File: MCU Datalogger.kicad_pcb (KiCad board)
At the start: 2 copper layers, 0 parts

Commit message: setup of pcbnew
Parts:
- added BT1: Battery_Cell, Connector_PinHeader_2.54mm:PinHeader_1x02_P2.54mm_Vertical, F.Cu at (160.0, 89.1)
- added C1: 22pF, Capacitor_SMD:C_0805_2012Metric, F.Cu at (155.5, 88.3)
- added C2: 22pF, Capacitor_SMD:C_0805_2012Metric, F.Cu at (155.5, 91.4)
- added C3: 0.1uF, Capacitor_SMD:C_0805_2012Metric, F.Cu at (155.5, 94.4)
- added C4: 0.1u, Capacitor_SMD:C_0805_2012Metric, F.Cu at (155.5, 97.4)
- added C5: 100 nF, Capacitor_SMD:CP_Elec_3x5.3, F.Cu at (161.1, 96.4)
- added D1: LED, LED_SMD:LED_0805_2012Metric, F.Cu at (164.6, 88.4)
- added D2: LED, LED_SMD:LED_0805_2012Metric, F.Cu at (164.6, 91.4)
- added H1: MountingHole, MountingHole:MountingHole_2.1mm, F.Cu at (137.6, 89.7)
- added H2: MountingHole, MountingHole:MountingHole_2.1mm, F.Cu at (137.6, 95.5)
- added H3: MountingHole, MountingHole:MountingHole_2.1mm, F.Cu at (137.6, 101.2)
- added H4: MountingHole, MountingHole:MountingHole_2.1mm, F.Cu at (137.6, 107.0)
- added J1: Conn_01x04_Pin, Connector_PinHeader_2.54mm:PinHeader_1x04_P2.54mm_Vertical, F.Cu at (175.8, 89.1)
- added J2: Conn_01x04_Pin, Connector_PinHeader_2.54mm:PinHeader_1x04_P2.54mm_Vertical, F.Cu at (180.4, 89.1)
- added J3: Conn_01x09_Pin, Connector_PinHeader_2.54mm:PinHeader_1x09_P2.54mm_Vertical, F.Cu at (171.2, 89.1)
- added J4: Conn_02x03_Odd_Even, Connector_PinHeader_2.54mm:PinHeader_2x03_P2.54mm_Vertical, F.Cu at (175.8, 101.3)
- added R1: 10k, Resistor_SMD:R_0805_2012Metric, F.Cu at (142.6, 88.3)
- added R2: 330, Resistor_SMD:R_0805_2012Metric, F.Cu at (142.6, 91.3)
- added R3: 4.7k, Resistor_SMD:R_0805_2012Metric, F.Cu at (142.6, 94.2)
- added R4: 4.7k, Resistor_SMD:R_0805_2012Metric, F.Cu at (142.6, 97.2)
- added R5: 10k, Resistor_SMD:R_0805_2012Metric, F.Cu at (142.6, 100.1)
- added R6: 10k, Resistor_SMD:R_0805_2012Metric, F.Cu at (142.6, 103.1)
- added R7: 330, Resistor_SMD:R_0805_2012Metric, F.Cu at (142.6, 106.0)
- added U1: 24LC1025, Package_SO:SOIC-8_3.9x4.9mm_P1.27mm, F.Cu at (149.1, 90.2)
- added U2: DS1337S_, ds1337s:SOIC127P600X175-8N, F.Cu at (161.8, 113.0)
- added U3: 24LC1025, Package_SO:SOIC-8_3.9x4.9mm_P1.27mm, F.Cu at (149.1, 96.8)
- added U4: ATMEGA328P-AU, footprints:TQFP32_32A_MCH, F.Cu at (150.7, 106.0)
- added Y1: 32.768 KHZ, Crystal:Crystal_SMD_5032-2Pin_5.0x3.2mm_HandSoldering, F.Cu at (161.8, 102.4)
- added Y2: 16 MHZ, Crystal:Crystal_SMD_5032-2Pin_5.0x3.2mm_HandSoldering, F.Cu at (161.8, 107.3)

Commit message: placed components
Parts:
- moved H4 46.5 mm to (179.8, 87.6)
- moved H3 44.4 mm to (179.8, 114.8)
- moved J3 38.2 mm to (142.2, 114.0), turned to 90 degrees
- moved R7 30.2 mm to (171.3, 96.5)
- moved R2 30.1 mm to (171.3, 100.3)
- moved R4 29.7 mm to (171.3, 89.4)
- moved J2 28.0 mm to (167.6, 114.0), turned to 90 degrees
- moved R3 24.8 mm to (167.0, 89.4), turned to 180 degrees
- moved Y1 23.8 mm to (138.2, 105.7), turned to 90 degrees
- moved BT1 22.5 mm to (138.3, 95.0)
- moved H2 19.3 mm to (137.7, 114.8)
- moved U2 16.9 mm to (145.7, 107.7)
- moved R5 16.6 mm to (156.6, 109.2)
- moved C2 16.2 mm to (162.6, 105.9), turned to 180 degrees
- moved C1 15.9 mm to (162.6, 102.6), turned to 180 degrees
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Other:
- board outline added: 47.5 x 32.5 mm

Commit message: Routing done and fixed the drc errors successfully
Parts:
- added REF**: KiCad-Logo2_5mm_SilkScreen, Symbol:KiCad-Logo2_5mm_SilkScreen, F.Cu at (170.5, 108.8)
- turned D1 to 180 degrees
- turned D2 to 180 degrees
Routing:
- net GND: track 0.00 -> 147.4 mm, vias 0 -> 6
- net /SCK: track 0.00 -> 145.7 mm, vias 0 -> 7
- net /vcc: track 0.00 -> 133.1 mm
- net /SDA: track 0.00 -> 81.0 mm, vias 0 -> 5
- net Net-(BT1-+): track 0.00 -> 69.6 mm, vias 0 -> 1
- net /RESET: track 0.00 -> 51.4 mm, vias 0 -> 3
- net /MISO: track 0.00 -> 46.7 mm, vias 0 -> 1
- net /MOSI: track 0.00 -> 46.3 mm, vias 0 -> 1
- net /D2: track 0.00 -> 42.8 mm, vias 0 -> 1
- net /TX: track 0.00 -> 34.6 mm, vias 0 -> 1
- net /RX: track 0.00 -> 33.4 mm, vias 0 -> 1
- net /D3: track 0.00 -> 31.1 mm, vias 0 -> 1
- net /D4: track 0.00 -> 29.9 mm, vias 0 -> 1
- net Net-(U4-PB6(PCINT6/XTAL1/TOSC1)): track 0.00 -> 22.8 mm
- net /D5: track 0.00 -> 16.5 mm, vias 0 -> 1
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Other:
- outline, holes or cut-outs redrawn

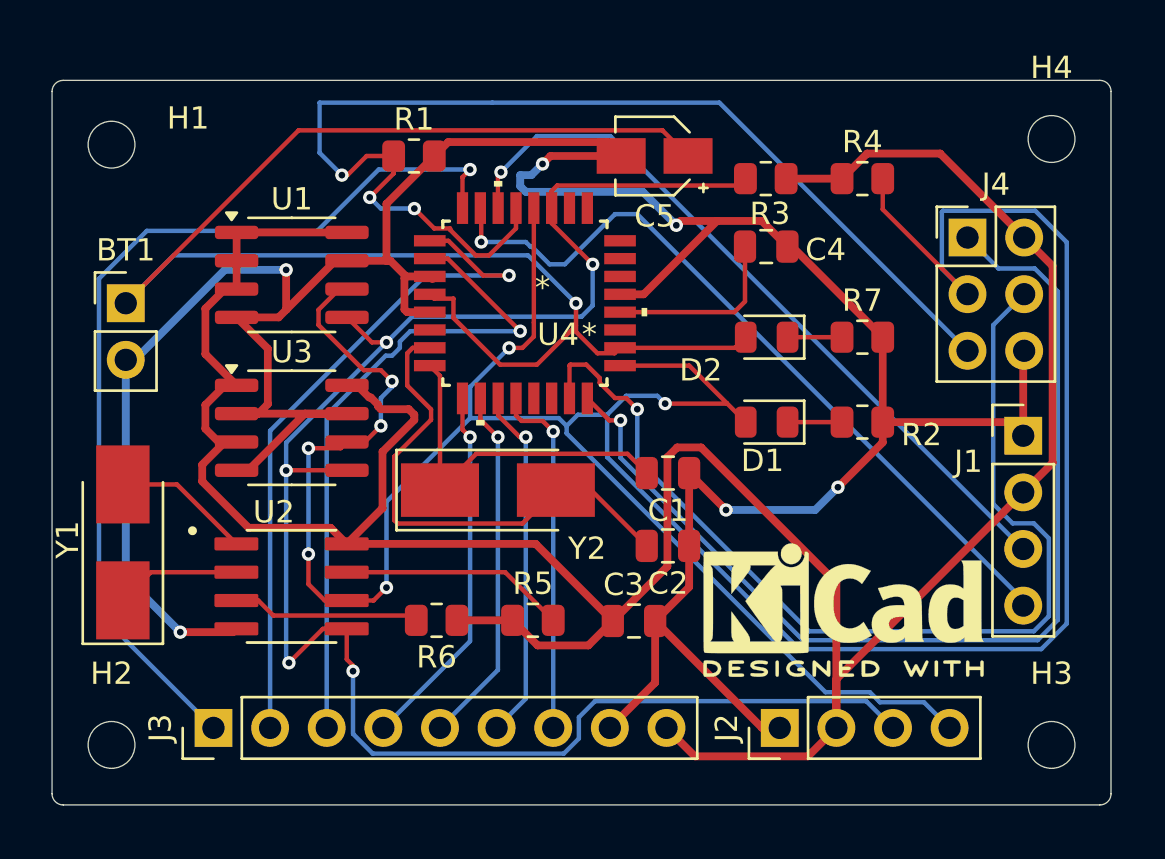
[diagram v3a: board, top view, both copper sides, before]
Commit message: copper fill and drc and refining the edge cuts completed
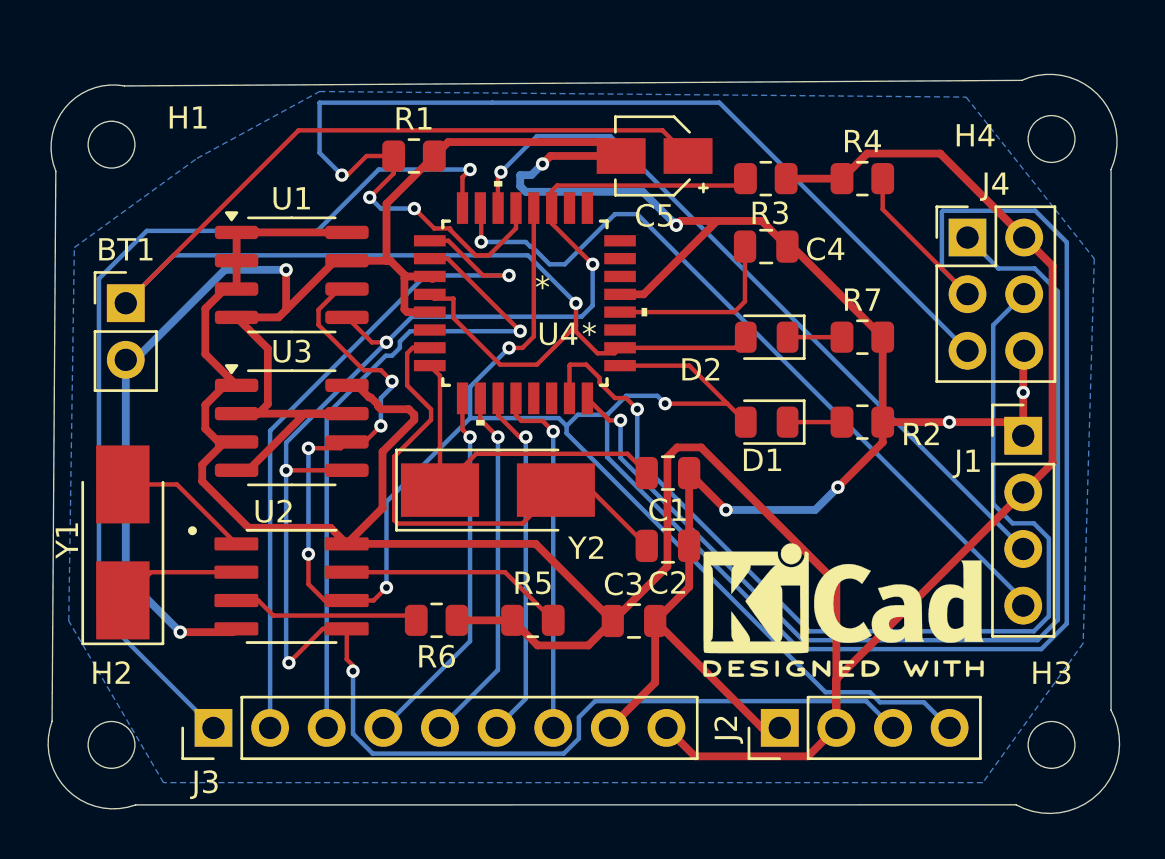
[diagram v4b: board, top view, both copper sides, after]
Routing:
- net GND: vias 6 -> 8
- added copper zone on B.Cu, net GND
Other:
- board size 47.5 x 32.5 mm -> 48.1 x 33.1 mm
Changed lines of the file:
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@@
 		(tags "Through hole pin header THT 1x09 2.54mm single row")
 		(property "Reference" "J3"
-			(at 0 -2.38 90)
+			(at -2.454 -0.34 180)
 			(layer "F.SilkS")
 			(effects
@@
 		(tags "mounting hole 2.1mm no annular")
 		(property "Reference" "H4"
-			(at 0 -3.2 0)
+			(at -3.432 -0.13 0)
 			(layer "F.SilkS")
 			(effects
@@
 	)
 	(gr_arc
-		(start 135 85.5)
-		(mid 135.146447 85.146447)
-		(end 135.5 85)
+		(start 182.5 113.25)
+		(mid 181.961345 116.96866)
+		(end 178.240926 117.495031)
 		(stroke
 			(width 0.05)
@@
 		(layer "Edge.Cuts")
 	)
-	(gr_line
-		(start 182 85)
-		(end 135.5 85)
+	(gr_arc
+		(start 138.75 117.5)
+		(mid 135.679513 116.817748)
+		(end 135.001326 113.74636)
 		(stroke
 			(width 0.05)
@@
 	)
 	(gr_line
-		(start 182.5 117)
-		(end 182.5 85.5)
+		(start 178.5 85)
+		(end 138.25 85.25)
 		(stroke
 			(width 0.05)
@@
 		(layer "Edge.Cuts")
 	)
-	(gr_arc
-		(start 182 85)
-		(mid 182.353553 85.146447)
-		(end 182.5 85.5)
+	(gr_line
+		(start 182.5 113.25)
+		(end 182.5 89)
 		(stroke
 			(width 0.05)
@@
 	)
 	(gr_arc
-		(start 135.5 117.5)
-		(mid 135.146447 117.353553)
-		(end 135 117)
+		(start 135.168862 89.072487)
+		(mid 135.573848 86.2459)
+		(end 138.25 85.25)
 		(stroke
 			(width 0.05)
@@
 	)
 	(gr_line
-		(start 135 85.5)
-		(end 135 117)
+		(start 135.168863 89.072487)
+		(end 135.001326 113.746364)
 		(stroke
 			(width 0.05)
@@
 	)
 	(gr_line
-		(start 135.5 117.5)
-		(end 182 117.5)
+		(start 138.75 117.5)
+		(end 178.240926 117.495031)
 		(stroke
 			(width 0.05)
@@
 	)
 	(gr_arc
-		(start 182.5 117)
-		(mid 182.353553 117.353553)
-		(end 182 117.5)
+		(start 178.5 85)
+		(mid 181.886001 85.613999)
+		(end 182.5 89)
 		(stroke
 			(width 0.05)
@@
 	)
 	(segment
+		(start 178.562 99)
+		(end 178.562 97.17181)
+		(width 0.35)
+		(layer "F.Cu")
+		(net 2)
+	)
+	(segment
 		(start 168.195 92.456)
 		(end 172.259 96.52)
@@
 	)
 	(segment
+		(start 175.25 100.33)
+		(end 177.952 100.33)
+		(width 0.35)
+		(layer "F.Cu")
+		(net 2)
+	)
+	(segment
 		(start 161.5384 94.596001)
 		(end 164.829401 91.305)
@@
 	(segment
 		(start 178.562 100.94)
-		(end 178.562 97.17181)
+		(end 178.562 99)
 		(width 0.35)
 		(layer "F.Cu")
@@
 	(segment
 		(start 172.259 100.33)
-		(end 177.952 100.33)
+		(end 175.25 100.33)
 		(width 0.35)
 		(layer "F.Cu")
@@
 	)
 	(via
+		(at 175.25 100.33)
+		(size 0.6)
+		(drill 0.3)
+		(layers "F.Cu" "B.Cu")
+		(net 2)
+	)
+	(via
 		(at 165.23 104.27)
 		(size 0.6)
@@
 		(net 2)
 	)
+	(via
+		(at 178.562 99)
+		(size 0.6)
+		(drill 0.3)
+		(layers "F.Cu" "B.Cu")
+		(net 2)
+	)
 	(segment
 		(start 156.5 89.25)
@@
 		(net 26)
 	)
+	(zone
+		(net 2)
+		(net_name "GND")
+		(layer "B.Cu")
+		(hatch full 0.5)
+		(connect_pads
+			(clearance 0.5)
+		)
+		(min_thickness 0.25)
+		(filled_areas_thickness no)
+		(fill yes
+			(mode hatch)
+			(thermal_gap 0.5)
+			(thermal_bridge_width 0.5)
+			(hatch_thickness 1)
+			(hatch_gap 1.5)
+			(hatch_orientation 0)
+			(hatch_border_algorithm hatch_thickness)
+			(hatch_min_hole_area 0.3)
+		)
+		(polygon
+			(pts
+				(xy 141.5 88.5) (xy 147 85.5) (xy 176 85.75) (xy 181.75 93) (xy 181.25 110.25) (xy 176.75 116.5)
+				(xy 140 116.5) (xy 135.75 109.25) (xy 136 92.5)
+			)
+		)
+	)
 	(embedded_fonts no)

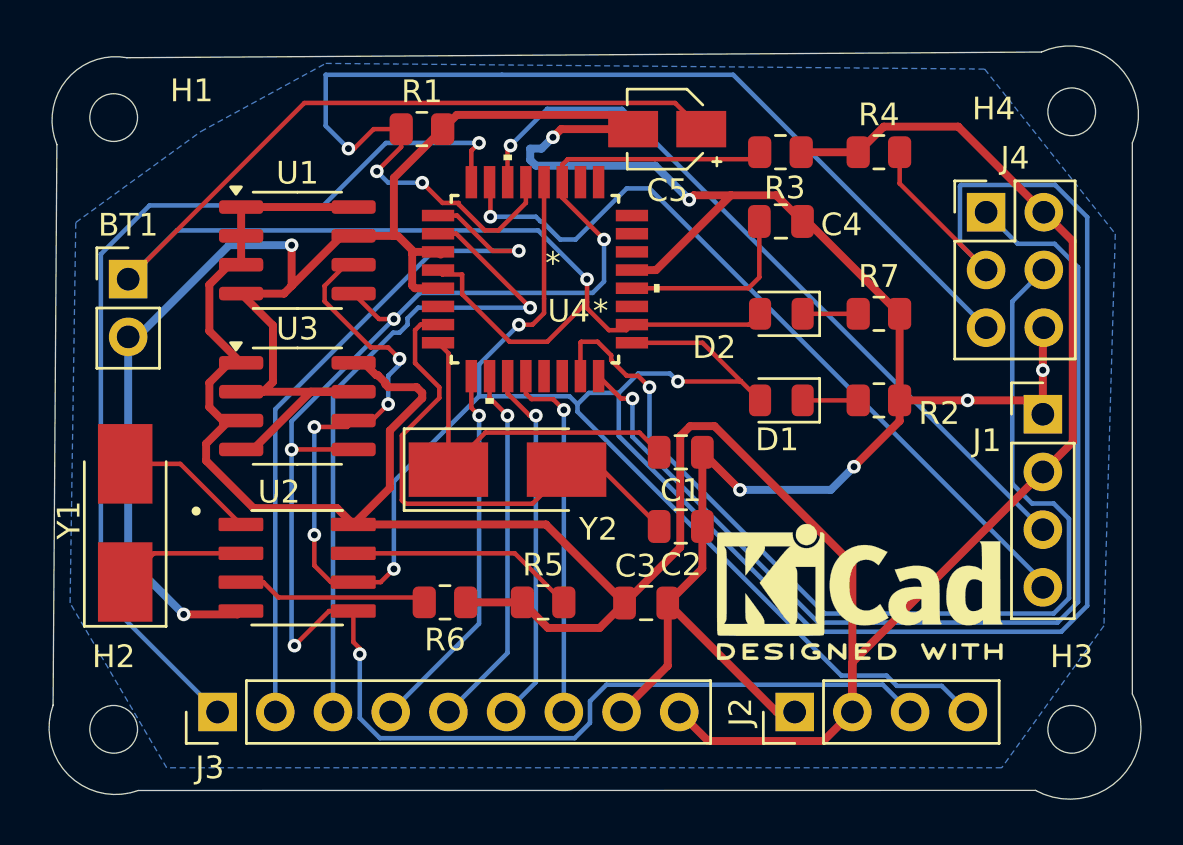
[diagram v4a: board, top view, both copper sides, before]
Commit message: arranged route tracks
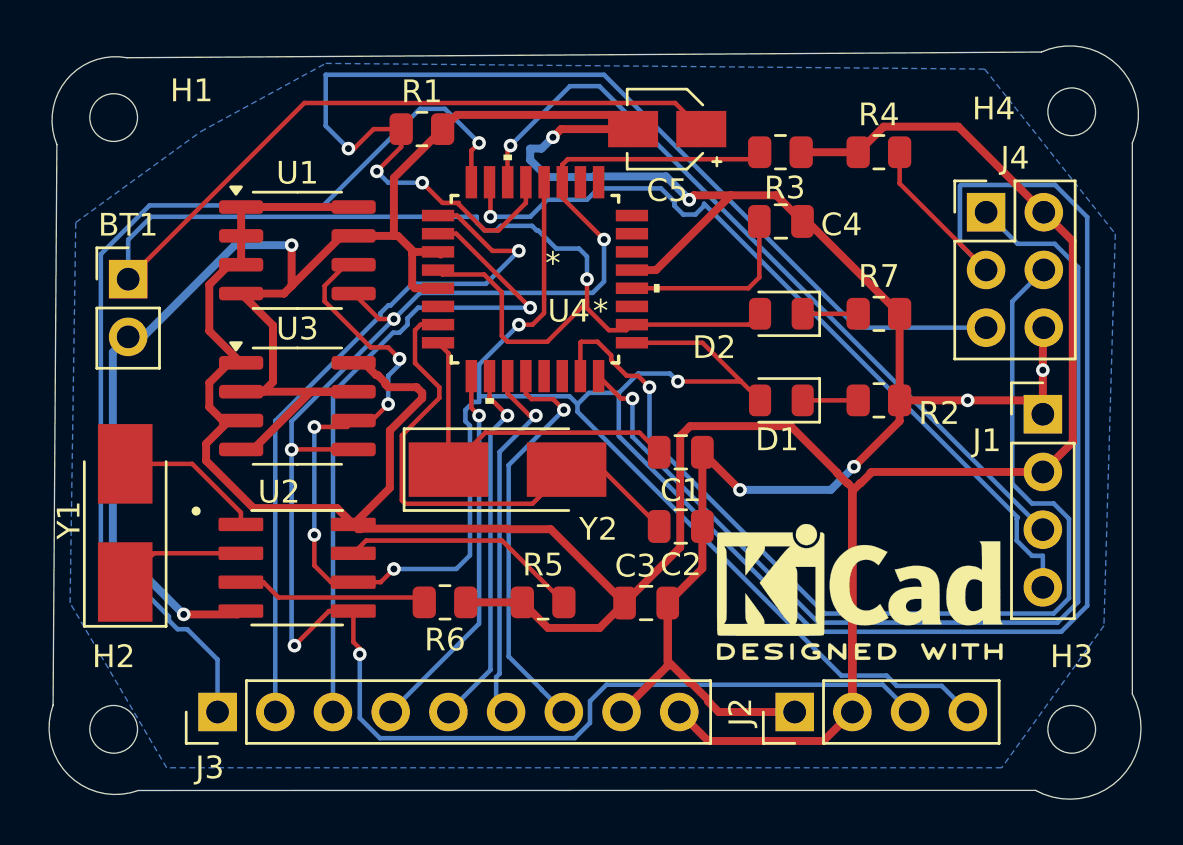
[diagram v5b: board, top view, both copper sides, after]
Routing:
- net /vcc: track 133.1 -> 139.6 mm
- net Net-(BT1-+): track 69.6 -> 72.6 mm
- net GND: track 147.4 -> 149.5 mm
- net /D8: track 16.0 -> 18.0 mm
- net /SCK: track 145.7 -> 147.6 mm
- net /D2: track 42.8 -> 44.3 mm
- net /TX: track 34.6 -> 35.7 mm
- net /RX: track 33.4 -> 34.3 mm

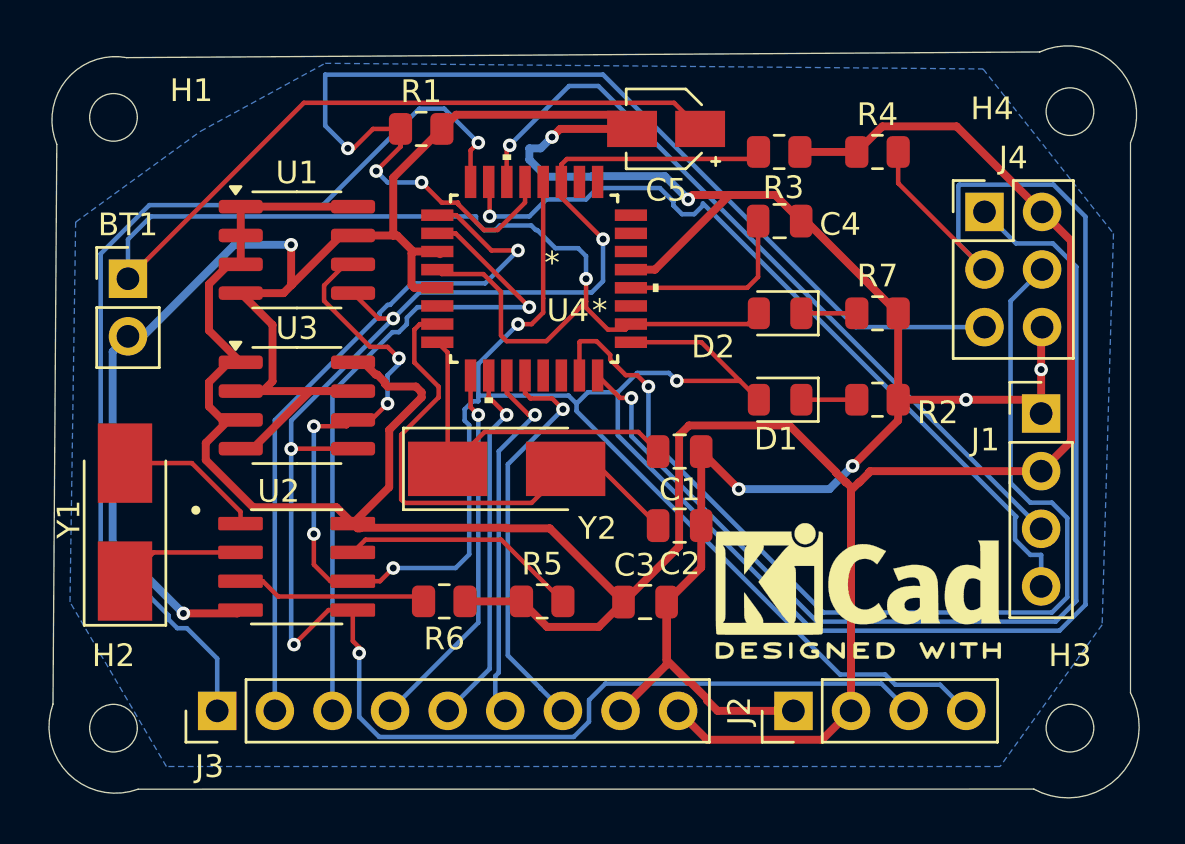
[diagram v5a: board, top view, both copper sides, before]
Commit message: arranged route track and later the schematics there was small mistkae so arranged and routed successfully preparation for manufacturing
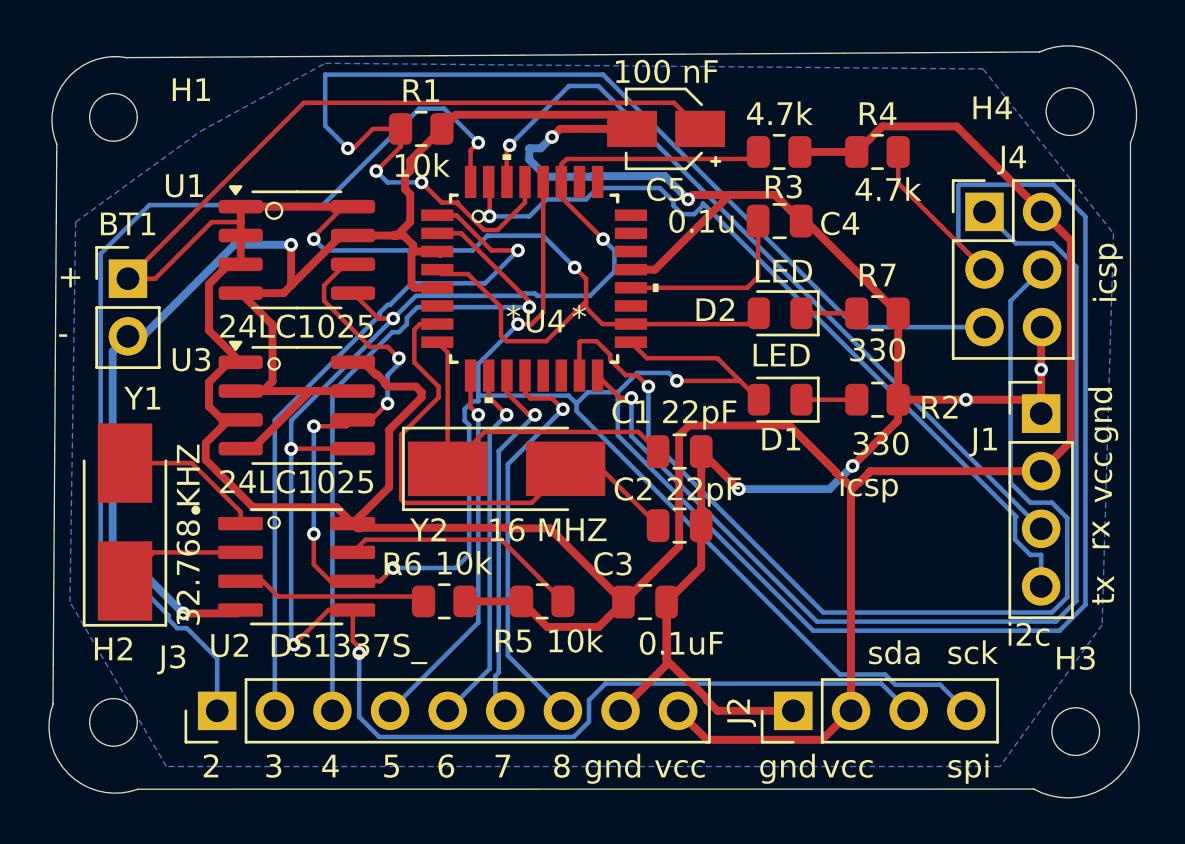
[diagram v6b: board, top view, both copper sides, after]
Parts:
- REF**: moved to B.Cu
- moved REF** 0.90 mm to (170.0, 108.0), turned to 180 degrees
- moved H3 0.30 mm to (180.1, 115.0)
- moved H2 0.25 mm to (137.7, 114.6)
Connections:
- BT1 pad 1: Net-(BT1-+) -> /vcc
- C5 pad 1: Net-(BT1-+) -> /vcc
- D2 pad 2: Net-(BT1-+) -> /vcc
- U4 pad 18: Net-(BT1-+) -> /vcc
- U4 pad 4: Net-(BT1-+) -> /vcc
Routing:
- net Net-(BT1-+): track 72.6 -> 0.00 mm, vias 1 -> 0
- net /vcc: track 139.6 -> 208.8 mm, vias 0 -> 2
- net /SDA: track 81.0 -> 81.6 mm
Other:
- board text added: "+"
- board text added: "-"
- board text added: "2"
- board text added: "3"
- board text added: "4"
- board text added: "5"
- board text added: "6"
- board text added: "7"
- board text added: "8"
- board text added: "gnd"
- board text added: "i2c"
- board text added: "icsp"
- board text added: "rx"
- board text added: "sck"
- board text added: "sda"
- board text added: "spi"
- board text added: "tx"
- board text added: "vcc"
